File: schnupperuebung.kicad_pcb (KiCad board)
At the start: 2 copper layers, 29.5 x 30.3 mm, 5 parts, among them J3 USB_C_Receptacle_PowerOnly_6P

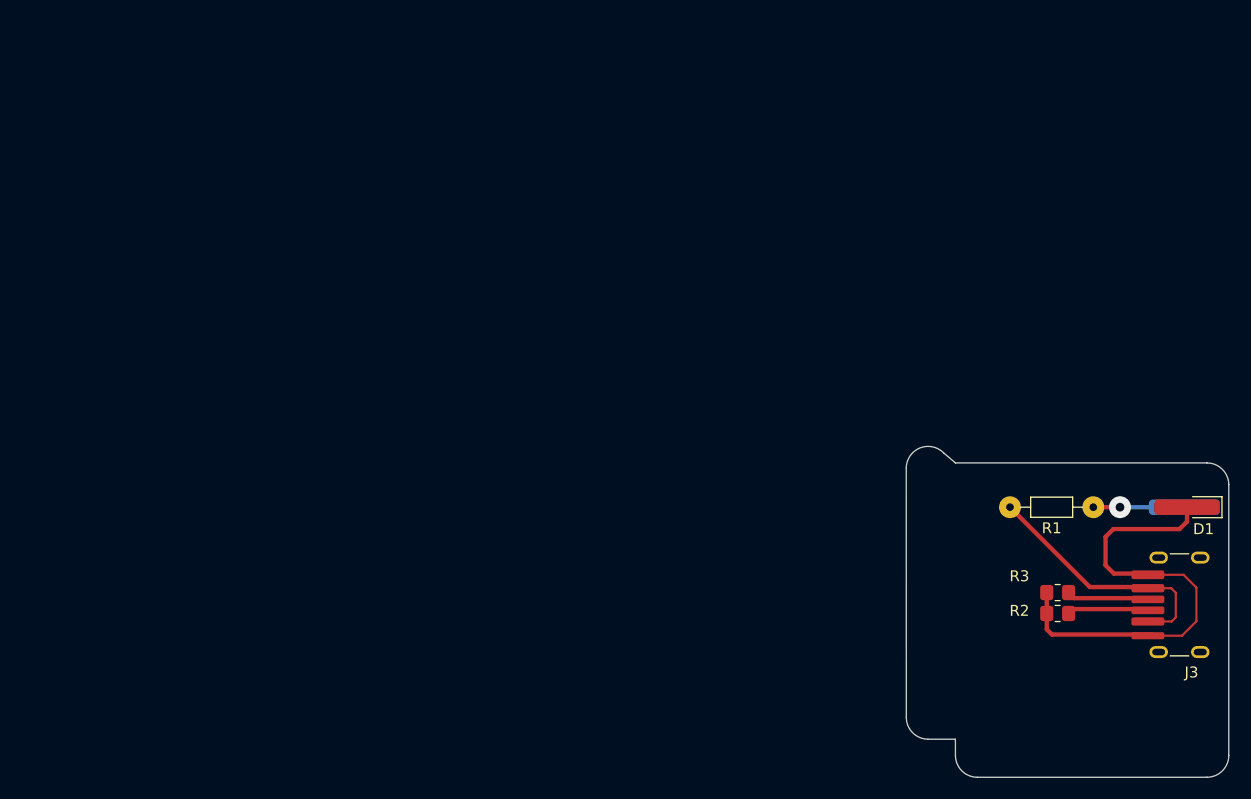
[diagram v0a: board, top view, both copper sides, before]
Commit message: Updated Footprint & Created pics
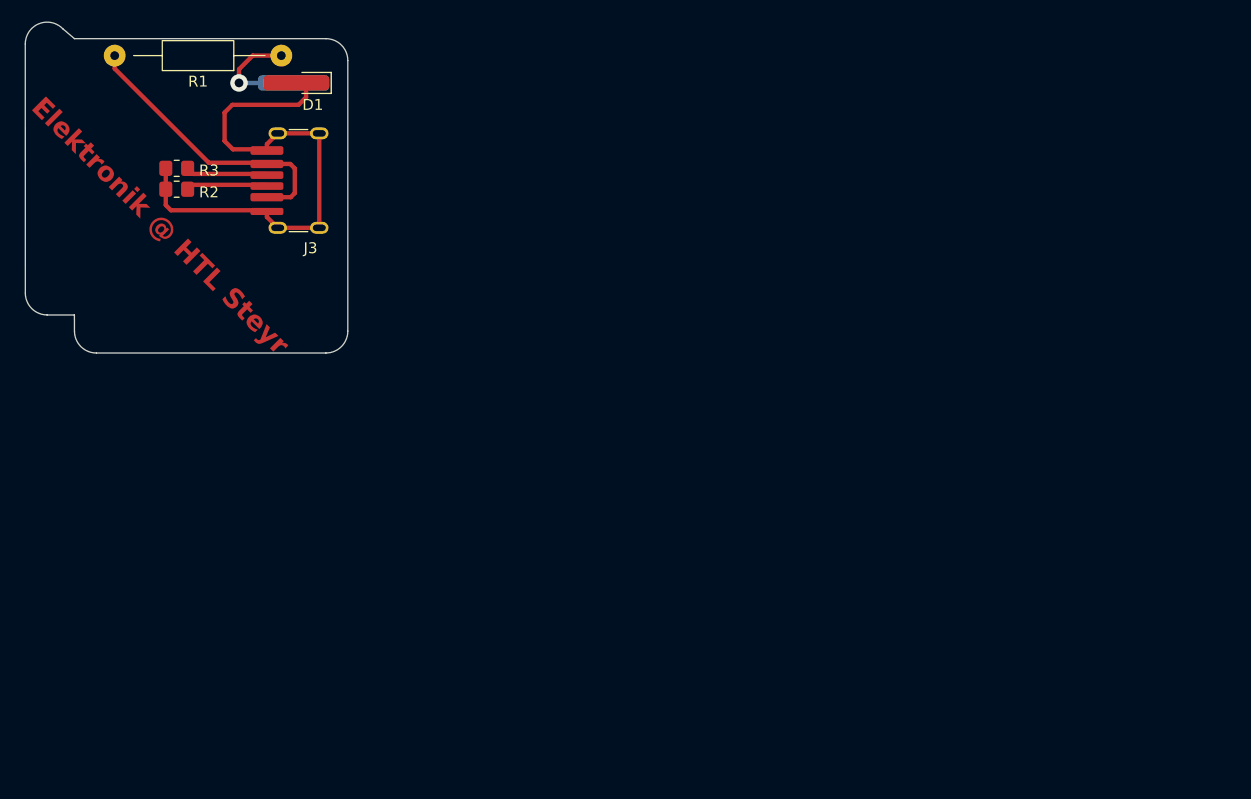
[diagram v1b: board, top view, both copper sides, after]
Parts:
- R1: footprint Resistor_THT:R_Axial_DIN0204_L3.6mm_D1.6mm_P7.62mm_Horizontal -> Resistor_THT:R_Axial_DIN0207_L6.3mm_D2.5mm_P15.24mm_Horizontal
- moved D1 90.2 mm to (110.4, 58.2)
- moved R2 89.4 mm to (98.0, 67.9)
- moved R3 89.4 mm to (98.0, 66.0)
- moved J3 89.4 mm to (110.2, 67.1)
- moved R1 85.0 mm to (107.5, 55.7)
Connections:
- net Net-(J3-VBUS-PadA9) renamed VBUS
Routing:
- net GND: track 42.9 -> 50.0 mm
- net Net-(D1-A): track 8.43 -> 11.6 mm
- net VBUS: track 24.8 -> 27.8 mm
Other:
- board text added: "Elektronik @ HTL Steyr"
- board text removed: "${REFERENCE}"
